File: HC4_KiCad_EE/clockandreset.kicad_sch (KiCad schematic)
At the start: 18 parts, among them IC15 74HC14, SW2 SW_Push, SW3 SW_Push, SW4 FreqSel, SW5 SW_SPDT

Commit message: たぶん完成！！！！！！！
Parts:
- SW4: value FreqSel -> SW_SPDT
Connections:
- net at R4.1, SW2.2: now also RN15.1 (R1.1); no longer RN15.3 (R3.1)
- net at LD46.2: now also RN15.3 (R3.1); no longer RN15.1 (R1.1)
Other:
- title: HC4_CPU -> HC4e_CPU
- moved on the sheet: RN15A, RN15C
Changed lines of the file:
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@@
 	(paper "A4")
 	(title_block
-		(title "HC4_CPU")
-		(date "2025-06-16")
+		(title "HC4e_CPU")
+		(date "2025-07-21")
 		(rev "1.0")
 	)
@@
 			)
 		)
-		(property "Value" "FreqSel"
+		(property "Value" "SW_SPDT"
 			(at 60.706 56.896 90)
 			(effects
@@
 	(symbol
 		(lib_id "Device:R_Pack04_Split")
-		(at 107.95 118.11 0)
+		(at 38.1 87.63 0)
 		(unit 1)
 		(exclude_from_sim no)
@@
 		(fields_autoplaced yes)
 		(property "Reference" "RN15"
-			(at 110.49 116.8399 0)
+			(at 40.64 86.3599 0)
 			(effects
 				(font
@@
 		)
 		(property "Value" "1k"
-			(at 110.49 119.3799 0)
+			(at 40.64 88.8999 0)
 			(effects
 				(font
@@
 		)
 		(property "Footprint" "Resistor_SMD:R_Array_Convex_4x0603"
-			(at 105.918 118.11 90)
+			(at 36.068 87.63 90)
 			(effects
 				(font
@@
 		)
 		(property "Datasheet" "~"
-			(at 107.95 118.11 0)
+			(at 38.1 87.63 0)
 			(effects
 				(font
@@
 		)
 		(property "Description" "4 resistor network, parallel topology, split"
-			(at 107.95 118.11 0)
+			(at 38.1 87.63 0)
 			(effects
 				(font
@@
 	(symbol
 		(lib_id "Device:R_Pack04_Split")
-		(at 38.1 87.63 0)
+		(at 107.95 118.11 0)
 		(unit 3)
 		(exclude_from_sim no)
@@
 		(fields_autoplaced yes)
 		(property "Reference" "RN15"
-			(at 40.64 86.3599 0)
+			(at 110.49 116.8399 0)
 			(effects
 				(font
@@
 		)
 		(property "Value" "1k"
-			(at 40.64 88.8999 0)
+			(at 110.49 119.3799 0)
 			(effects
 				(font
@@
 		)
 		(property "Footprint" "Resistor_SMD:R_Array_Convex_4x0603"
-			(at 36.068 87.63 90)
+			(at 105.918 118.11 90)
 			(effects
 				(font
@@
 		)
 		(property "Datasheet" "~"
-			(at 38.1 87.63 0)
+			(at 107.95 118.11 0)
 			(effects
 				(font
@@
 		)
 		(property "Description" "4 resistor network, parallel topology, split"
-			(at 38.1 87.63 0)
-			(effects
-				(font
+			(at 107.95 118.11 0)
+			(effects
+				(font

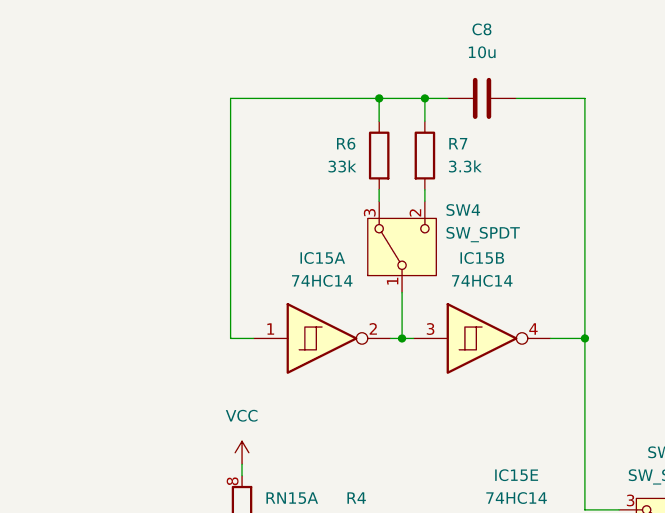
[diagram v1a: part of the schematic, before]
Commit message: 妥協に妥協を重ね妥協を加速する あとクロックの起動が安定しないのを直した
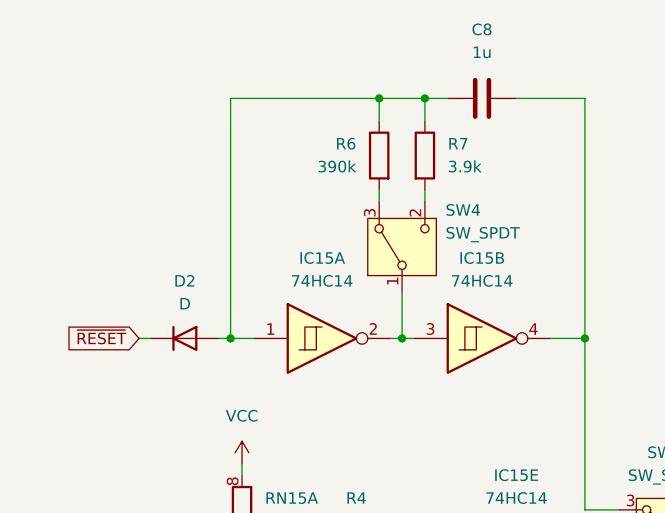
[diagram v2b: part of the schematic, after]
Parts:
- added D2: D, Diode_SMD:D_SOD-323_HandSoldering, symbol Device:D
- C8: value 10u -> 1u
- R6: value 33k -> 390k
- R7: value 3.3k -> 3.9k
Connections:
- net ~{RESET}: now also D2.1 (K)
- net at C8.1, IC15.1, R6.1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: now also D2.2 (A)
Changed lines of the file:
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@@
 	)
 	(junction
+		(at 36.83 68.58)
+		(diameter 0)
+		(color 0 0 0 0)
+	)
+	(junction
 		(at 38.1 92.71)
 		(diameter 0)
@@
 	(wire
 		(pts
+			(xy 35.56 68.58) (xy 36.83 68.58)
+		)
+		(stroke
+			(width 0)
+			(type default)
+		)
+	)
+	(wire
+		(pts
 			(xy 38.1 151.13) (xy 38.1 152.4)
 		)
@@
 	(wire
 		(pts
+			(xy 26.67 68.58) (xy 27.94 68.58)
+		)
+		(stroke
+			(width 0)
+			(type default)
+		)
+	)
+	(wire
+		(pts
 			(xy 55.88 63.5) (xy 55.88 68.58)
 		)
@@
 	)
 	(global_label "~{RESET}"
+		(shape input)
+		(at 26.67 68.58 180)
+		(fields_autoplaced yes)
+		(effects
+			(font
+				(size 1.27 1.27)
+			)
+			(justify right)
+		)
+		(property "Intersheetrefs" "${INTERSHEET_REFS}"
+			(at 17.9397 68.58 0)
+			(effects
+				(font
+					(size 1.27 1.27)
+				)
+				(justify right)
+				(hide yes)
+			)
+		)
+	)
+	(global_label "~{RESET}"
 		(shape output)
 		(at 95.25 151.13 0)
@@
 			)
 		)
-		(property "Value" "10u"
+		(property "Value" "1u"
 			(at 64.77 36.83 90)
 			(effects
@@
 	)
 	(symbol
+		(lib_id "Device:D")
+		(at 31.75 68.58 0)
+		(unit 1)
+		(exclude_from_sim no)
+		(in_bom yes)
+		(on_board yes)
+		(dnp no)
+		(fields_autoplaced yes)
+		(property "Reference" "D2"
+			(at 31.75 62.23 0)
+			(effects
+				(font
+					(size 1.27 1.27)
+				)
+			)
+		)
+		(property "Value" "D"
+			(at 31.75 64.77 0)
+			(effects
+				(font
+					(size 1.27 1.27)
+				)
+			)
+		)
+		(property "Footprint" "Diode_SMD:D_SOD-323_HandSoldering"
+			(at 31.75 68.58 0)
+			(effects
+				(font
+					(size 1.27 1.27)
+				)
+				(hide yes)
+			)
+		)
+		(property "Datasheet" "~"
+			(at 31.75 68.58 0)
+			(effects
+				(font
+					(size 1.27 1.27)
+				)
+				(hide yes)
+			)
+		)
+		(property "Description" "Diode"
+			(at 31.75 68.58 0)
+			(effects
+				(font
+					(size 1.27 1.27)
+				)
+				(hide yes)
+			)
+		)
+		(property "Sim.Device" "D"
+			(at 31.75 68.58 0)
+			(effects
+				(font
+					(size 1.27 1.27)
+				)
+				(hide yes)
+			)
+		)
+		(property "Sim.Pins" "1=K 2=A"
+			(at 31.75 68.58 0)
+			(effects
+				(font
+					(size 1.27 1.27)
+				)
+				(hide yes)
+			)
+		)
+		(pin "1"
+		)
+		(pin "2"
+		)
+		(instances
+			(project ""
+				(path "/33731ded-38c0-4297-bdd8-92b082f46ff8/3d67359d-c55c-4207-8a6b-ff7c83e276f6"
+					(reference "D2")
+					(unit 1)
+				)
+			)
+		)
+	)
+	(symbol
 		(lib_id "power:GND")
 		(at 38.1 105.41 0)
@@
 			)
 		)
-		(property "Value" "3.3k"
+		(property "Value" "3.9k"
 			(at 60.96 49.5299 0)
 			(effects
@@
 			)
 		)
-		(property "Value" "33k"
+		(property "Value" "390k"
 			(at 50.8 49.5299 0)
 			(effects

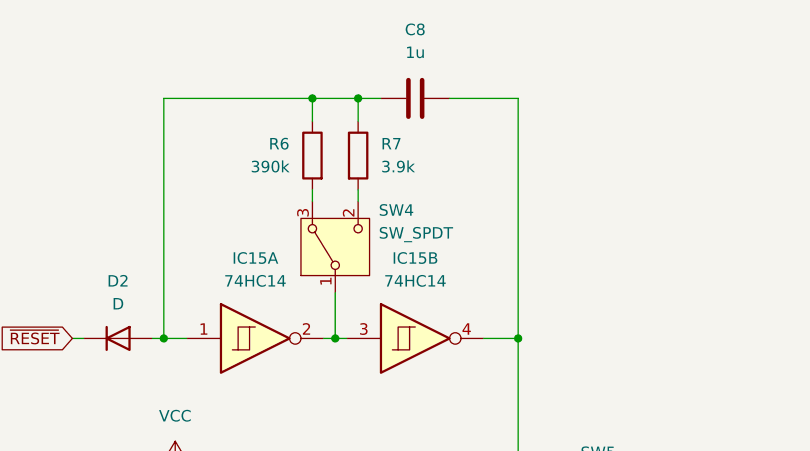
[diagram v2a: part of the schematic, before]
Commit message: Update KiCad project files and schematic components
- Changed active layer from 0 to 5 in HC4_KiCad_EE.kicad_prl.
- Adjusted minimum resolved spokes from 2 to 1 and updated solder mask clearance in HC4_KiCad_EE.kicad_pro.
- Corrected resistor value from "3.9k" to "390" in clockandreset.kicad_sch.
- Added fabrication toolkit options JSON file for project configuration.
- Modified LED component positions in instructiondecode.kicad_sch for better alignment.
- Created .gitignore file in production directory to exclude unnecessary files.
- Added HC4e_Rev01.zip to production directory for project release.
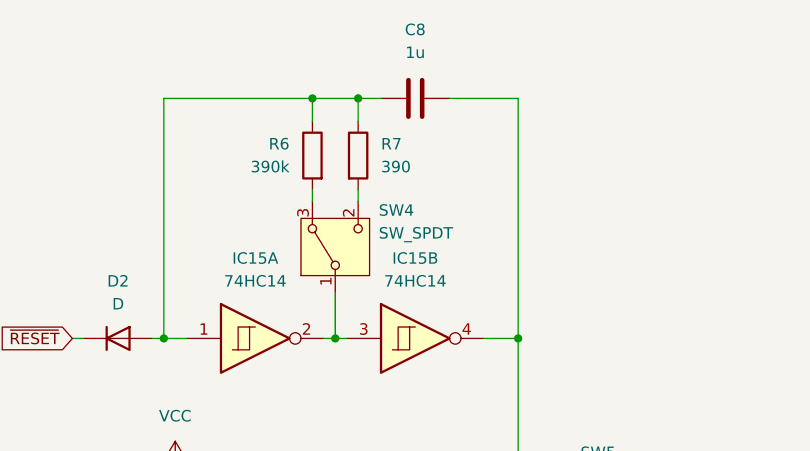
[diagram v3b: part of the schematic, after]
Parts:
- R7: value 3.9k -> 390
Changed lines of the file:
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@@
 			)
 		)
-		(property "Value" "3.9k"
+		(property "Value" "390"
 			(at 60.96 49.5299 0)
 			(effects

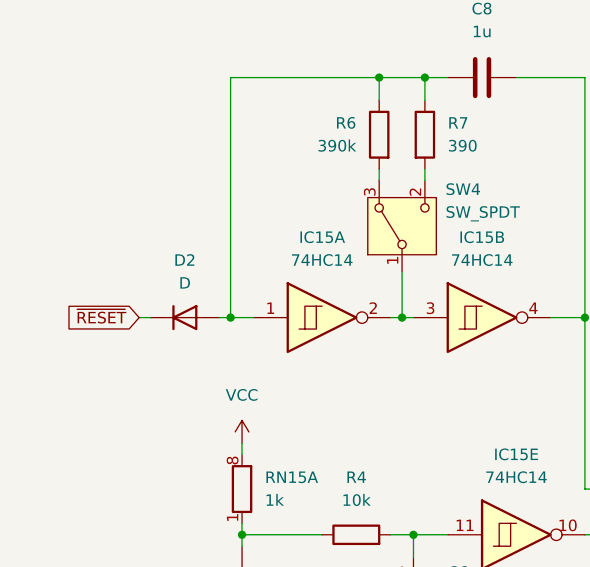
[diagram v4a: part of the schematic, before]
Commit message: MOSFETを回路上より排除
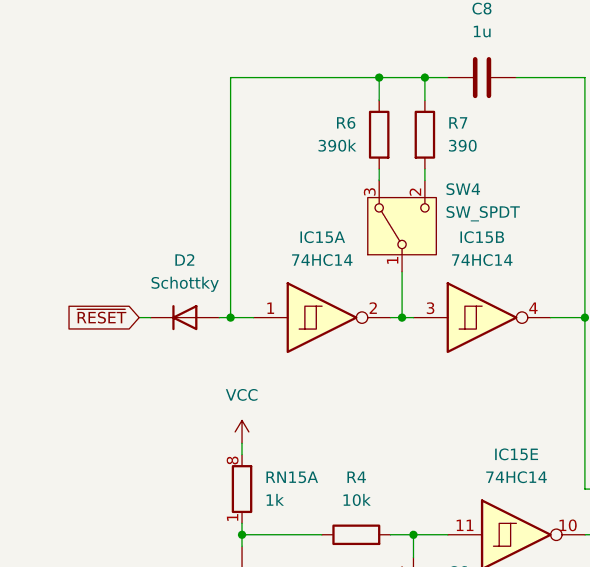
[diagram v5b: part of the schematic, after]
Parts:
- D2: value D -> Schottky
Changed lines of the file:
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@@
 			)
 		)
-		(property "Value" "D"
+		(property "Value" "Schottky"
 			(at 31.75 64.77 0)
 			(effects

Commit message: 2.0に改版
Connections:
- net at R4.1, SW2.2: now also RN15.2 (R2.1); no longer RN15.1 (R1.1)
- net at R5.1, SW3.2: now also RN15.1 (R1.1); no longer RN15.2 (R2.1)
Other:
- moved on the sheet: RN15A, RN15B
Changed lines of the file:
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@@
 	(title_block
 		(title "HC4e_CPU")
-		(date "2025-11-12")
-		(rev "1.2")
+		(date "2026-03-19")
+		(rev "2.0")
 	)
 	(junction
@@
 	(symbol
 		(lib_id "Device:R_Pack04_Split")
-		(at 38.1 146.05 0)
+		(at 38.1 87.63 0)
 		(unit 2)
 		(exclude_from_sim no)
@@
 		(fields_autoplaced yes)
 		(property "Reference" "RN15"
-			(at 40.64 144.7799 0)
+			(at 40.64 86.3599 0)
 			(effects
 				(font
@@
 		)
 		(property "Value" "1k"
-			(at 40.64 147.3199 0)
+			(at 40.64 88.8999 0)
 			(effects
 				(font
@@
 		)
 		(property "Footprint" "Resistor_SMD:R_Array_Convex_4x0603"
-			(at 36.068 146.05 90)
+			(at 36.068 87.63 90)
 			(effects
 				(font
@@
 		)
 		(property "Datasheet" "~"
-			(at 38.1 146.05 0)
+			(at 38.1 87.63 0)
 			(effects
 				(font
@@
 		)
 		(property "Description" "4 resistor network, parallel topology, split"
-			(at 38.1 146.05 0)
+			(at 38.1 87.63 0)
 			(effects
 				(font
@@
 	(symbol
 		(lib_id "Device:R_Pack04_Split")
-		(at 38.1 87.63 0)
+		(at 38.1 146.05 0)
 		(unit 1)
 		(exclude_from_sim no)
@@
 		(fields_autoplaced yes)
 		(property "Reference" "RN15"
-			(at 40.64 86.3599 0)
+			(at 40.64 144.7799 0)
 			(effects
 				(font
@@
 		)
 		(property "Value" "1k"
-			(at 40.64 88.8999 0)
+			(at 40.64 147.3199 0)
 			(effects
 				(font
@@
 		)
 		(property "Footprint" "Resistor_SMD:R_Array_Convex_4x0603"
-			(at 36.068 87.63 90)
+			(at 36.068 146.05 90)
 			(effects
 				(font
@@
 		)
 		(property "Datasheet" "~"
-			(at 38.1 87.63 0)
+			(at 38.1 146.05 0)
 			(effects
 				(font
@@
 		)
 		(property "Description" "4 resistor network, parallel topology, split"
-			(at 38.1 87.63 0)
-			(effects
-				(font
+			(at 38.1 146.05 0)
+			(effects
+				(font

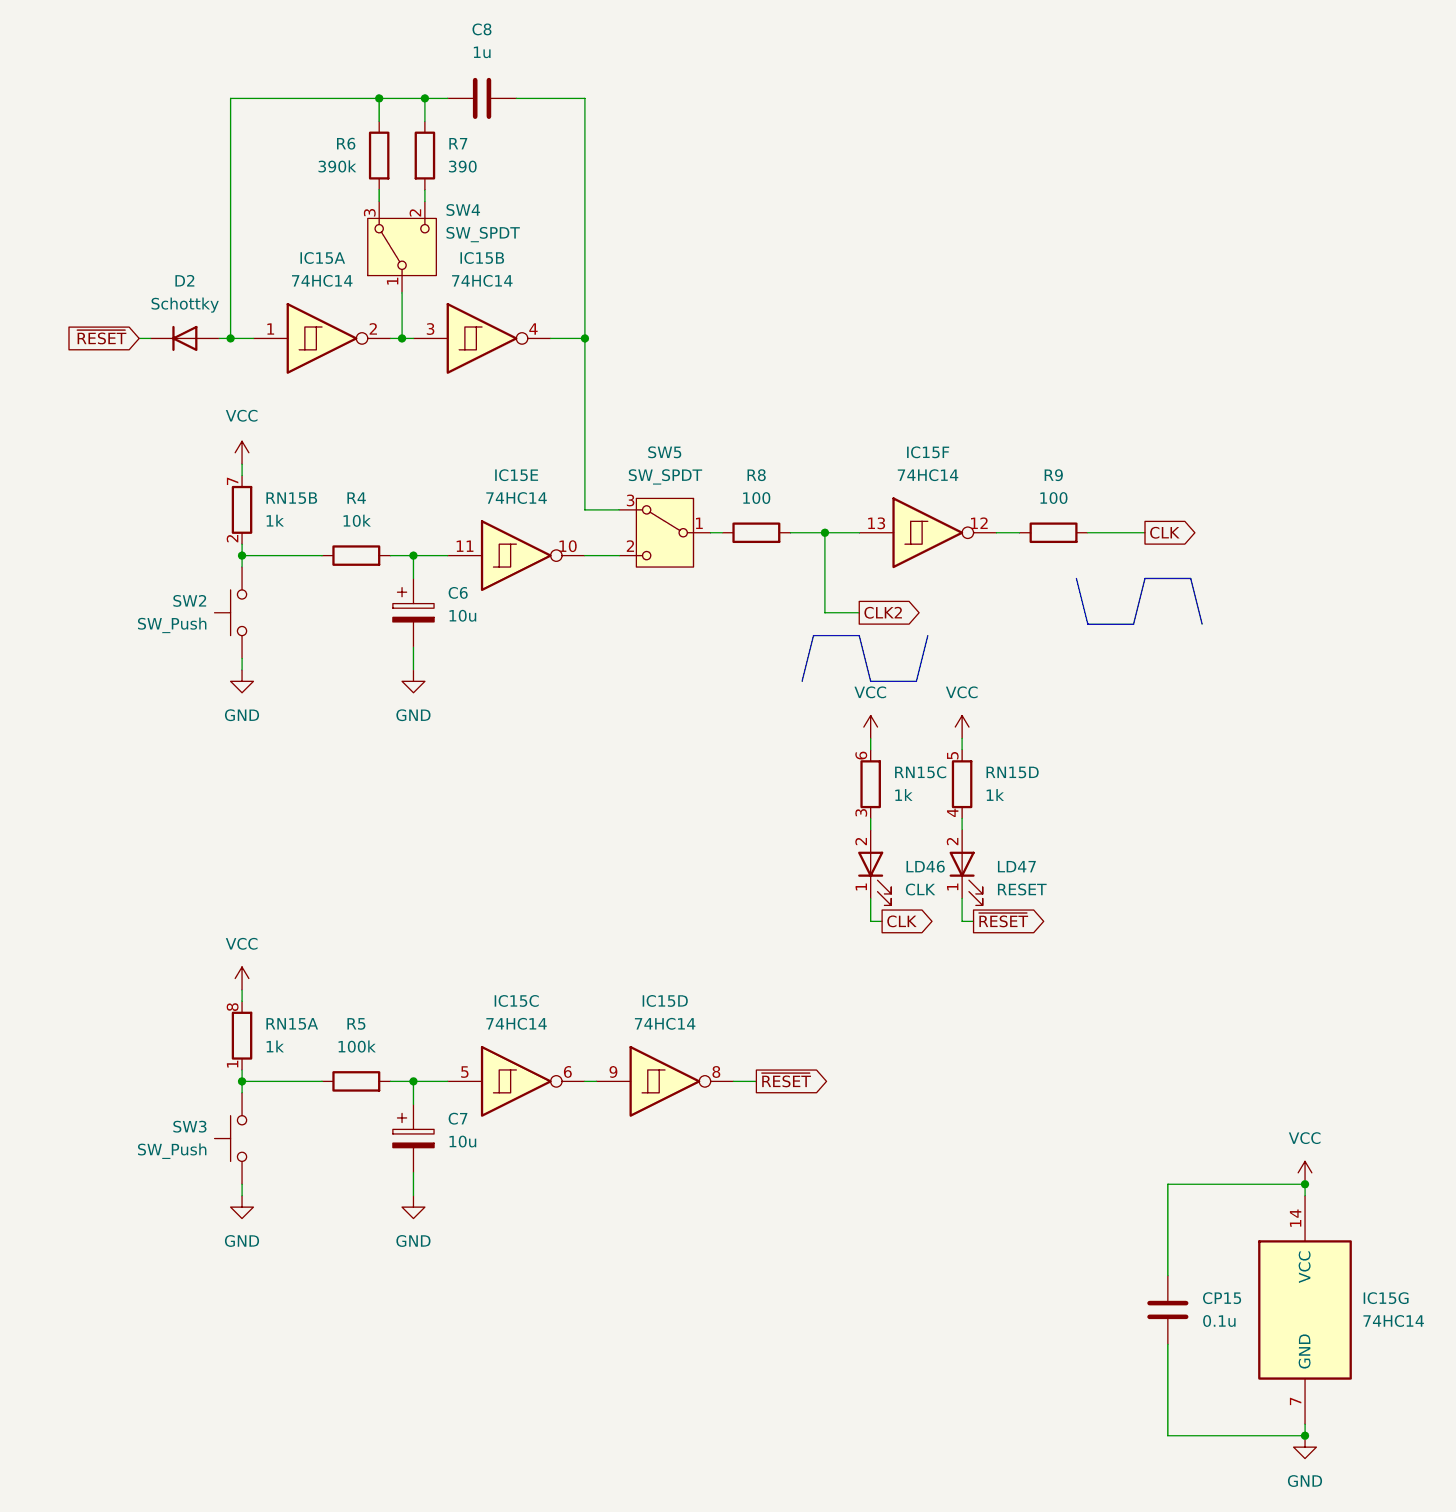
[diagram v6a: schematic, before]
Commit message: feat:HC4e改版,BOMを令和最新版に更新,KiCadを10に更新
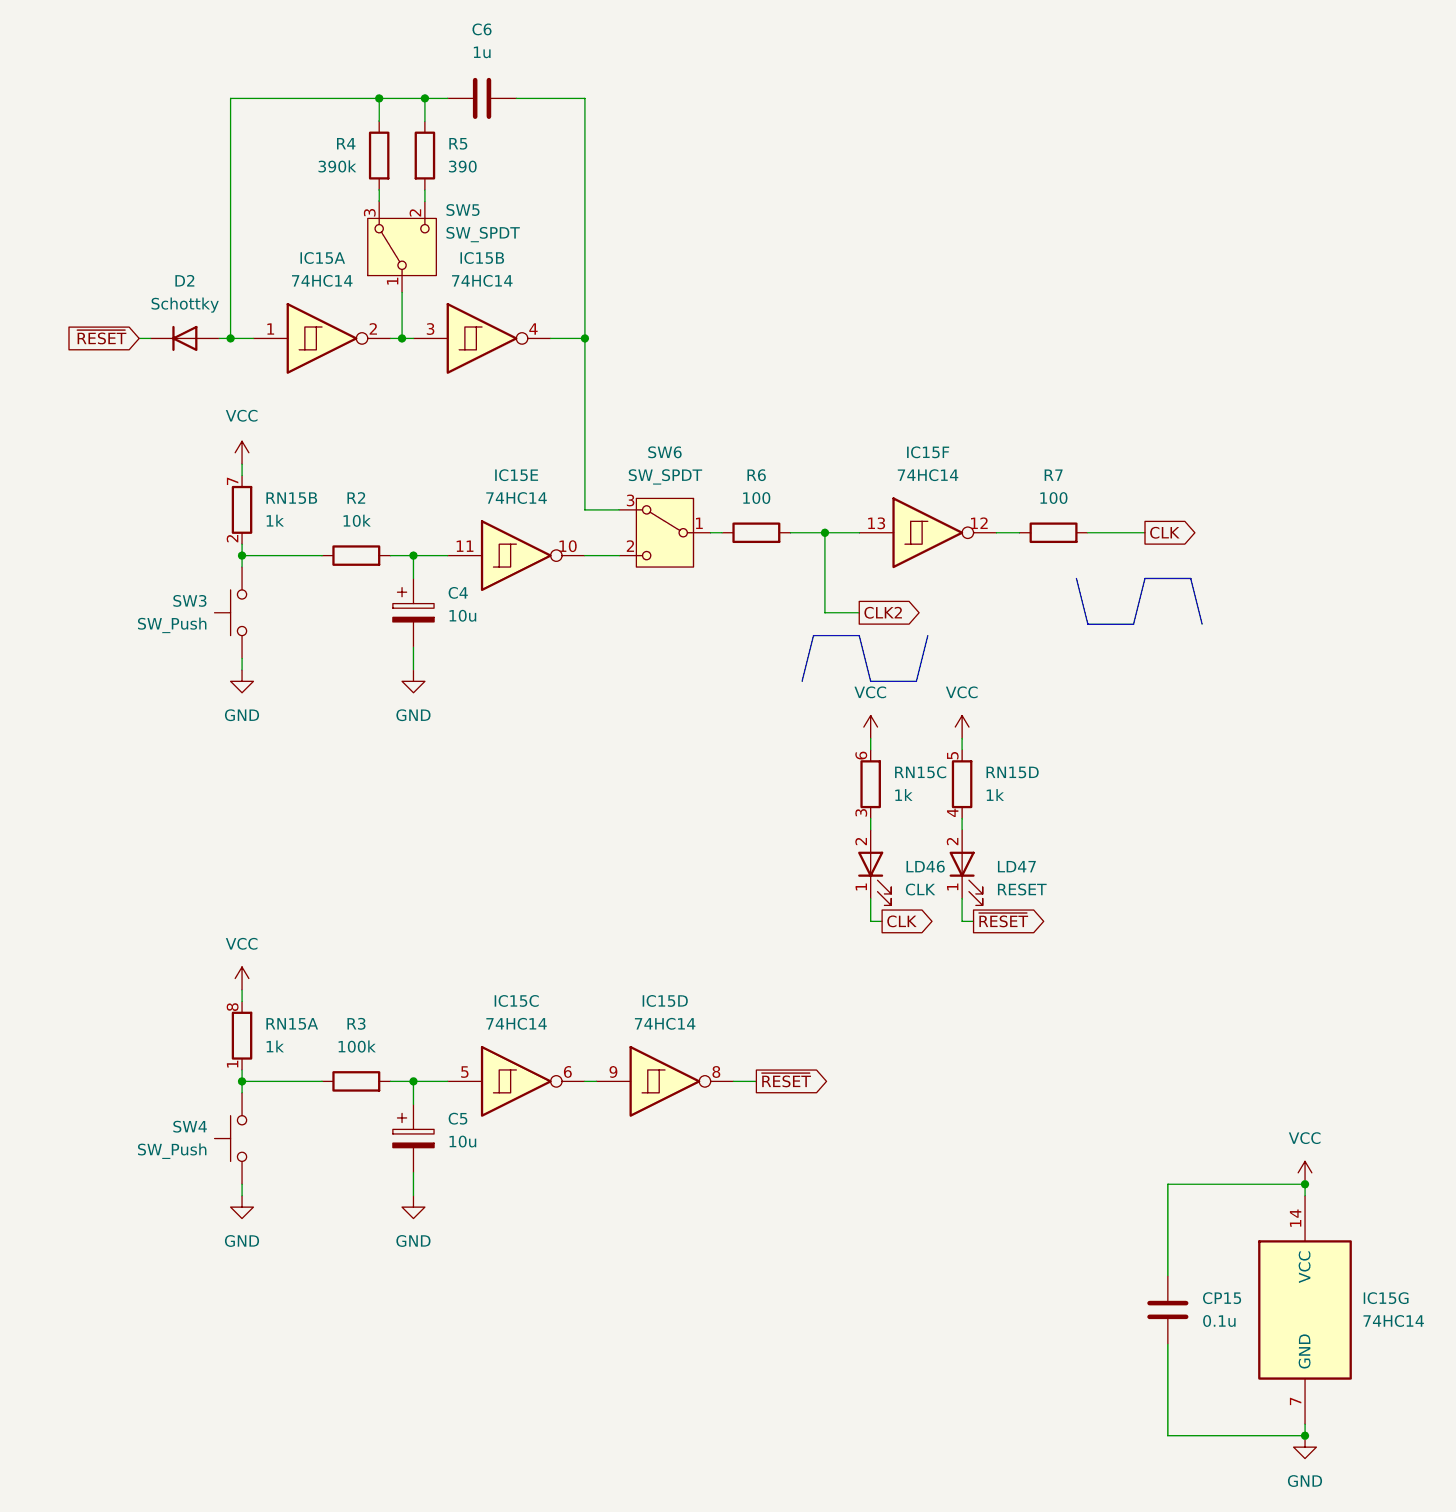
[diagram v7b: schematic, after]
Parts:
- renumbered C6 to C4, C7 to C5, C8 to C6, R4 to R2, R5 to R3, R6 to R4, R7 to R5, R8 to R6, R9 to R7, SW2 to SW3, SW3 to SW4, SW4 to SW5, SW5 to SW6
